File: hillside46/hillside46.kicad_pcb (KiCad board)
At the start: 2 copper layers, 142.5 x 99.9 mm, 92 parts, among them J1 Haptic, J2 TRRS, J3 Bat_Pos, J4 Bat_Neg, J5 Bat_Pos, J6 Bat_Neg, K1 SW_Key, K10 SW_Key, K11 SW_Key, K12 SW_Key, K13 SW_Key, K14 SW_Key, K15 SW_Key, K16 SW_Key, K17 SW_Key, K18 SW_Key, K19 SW_Rotary, K2 SW_Key, K20 SW_Rotary, K21 SW_Key, K22 SW_Key, K23 SW_Key, K3 SW_Key, K4 SW_Key, K5 SW_Key, K6 SW_Key, K7 SW_Key, K8 SW_Key, K9 SW_Key, SW1 SKQGAFE010, SW2 SW_Power, U1 ProMicro_r, U2 SRV05-4

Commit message: my mods
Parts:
- removed D1, D2, D3, D4: SK6812-MINI-E, hillside_basic:SK6812-MINI-E
- removed D19, D20, D21: BAV70, hillside_basic:SOT-23
- removed H1: Mount_Tenting, hillside:Tenting_Puck
- removed H26, H27, H28, H29, H30, H31: Breakoff Hole, hillside_basic:HoleBreakoff_1mm
- removed H3: Logo, hillside:Hillside_Logo
- added D16: 1N4148W, Diode_SMD:D_SOD-123, F.Cu at (89.6, 103.9)
- added D17: 1N4148W, Diode_SMD:D_SOD-123, F.Cu at (107.3, 100.7)
- added D18: 1N4148W, Diode_SMD:D_SOD-123, F.Cu at (124.0, 85.6)
- added D22: 1N4148W, Diode_SMD:D_SOD-123, F.Cu at (142.5, 78.5)
- added D23: 1N4148W, Diode_SMD:D_SOD-123, F.Cu at (160.5, 84.0)
- added D24: 1N4148W, Diode_SMD:D_SOD-123, F.Cu at (178.5, 69.6)
- added D25: 1N4148W, Diode_SMD:D_SOD-123, F.Cu at (178.5, 86.5)
- added D26: 1N4148W, Diode_SMD:D_SOD-123, F.Cu at (170.8, 104.0)
- added D27: 1N4148W, Diode_SMD:D_SOD-123, F.Cu at (190.3, 112.1)
- added D28: 1N4148W, Diode_SMD:D_SOD-123, F.Cu at (207.0, 125.0)
- added D29: 1N4148W, Diode_SMD:D_SOD-123, F.Cu at (198.8, 97.5)
- added D30: 1N4148W, Diode_SMD:D_SOD-123, F.Cu at (150.0, 101.0)
- added D5: 1N4148W, Diode_SMD:D_SOD-123, F.Cu at (83.7, 70.5)
- added D6: 1N4148W, Diode_SMD:D_SOD-123, F.Cu at (86.7, 87.2)
- D10, D11, D12, D13, D14, D15, D7, D8, D9: value BAV70 -> 1N4148W; footprint hillside_basic:SOT-23 -> Diode_SMD:D_SOD-123
- K19, K20: value SW_Rotary -> SW_Key; footprint hillside:pg1350-DR_rotary_hotswap -> hillside:pg1350-R_hotswap
- moved D13 79.2 mm to (160.5, 49.9), turned to 180 degrees
- moved D14 40.9 mm to (160.5, 67.0), turned to 180 degrees
- moved D9 39.5 mm to (121.0, 51.6), turned to -175 degrees
- moved D8 36.4 mm to (104.4, 84.0), turned to -170 degrees
- moved D15 36.3 mm to (178.5, 52.5), turned to 180 degrees
- moved D11 31.2 mm to (142.5, 44.5), turned to 180 degrees
- moved D10 23.8 mm to (122.5, 68.6), turned to -175 degrees
- moved D12 18.8 mm to (142.5, 61.5), turned to 180 degrees
- moved K20 4.51 mm to (150.0, 105.7), turned to 180 degrees
- moved K19 4.50 mm to (196.5, 101.5)
- turned D7 to -170 degrees
- turned K13 to -170 degrees
- turned K14 to -170 degrees
- turned K21 to 165 degrees
- turned K23 to 135 degrees
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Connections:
- D10 pad 1: Net-(D10-Pad1) -> row1
- D10 pad 2: Net-(D10-Pad2) -> Net-(D10-A)
- D11 pad 1: Net-(D11-Pad1) -> row0
- D11 pad 2: Net-(D11-Pad2) -> Net-(D11-A)
- D12 pad 1: Net-(D12-Pad1) -> row1
- D12 pad 2: Net-(D12-Pad2) -> Net-(D12-A)
- D13 pad 1: Net-(D13-Pad1) -> row0
- D13 pad 2: Net-(D13-Pad2) -> Net-(D13-A)
- D14 pad 1: Net-(D14-Pad1) -> row1
- D14 pad 2: Net-(D14-Pad2) -> Net-(D14-A)
- D15 pad 1: Net-(D15-Pad1) -> row0
- D15 pad 2: Net-(D15-Pad2) -> Net-(D15-A)
- D7 pad 1: Net-(D7-Pad1) -> row0
- D8 pad 1: Net-(D8-Pad1) -> row1
- D8 pad 2: Net-(D8-Pad2) -> Net-(D8-A)
- D9 pad 1: Net-(D9-Pad1) -> row0
- D9 pad 2: Net-(D9-Pad2) -> Net-(D9-A)
- JP2 pad 2: Net-(D19-Pad2) -> row3
- K1 pad 2: Net-(D7-Pad1) -> Net-(D5-A)
- K10 pad 2: Net-(D11-Pad2) -> Net-(D12-A)
- K11 pad 2: Net-(D12-Pad1) -> Net-(D14-A)
- K12 pad 2: Net-(D12-Pad2) -> Net-(D24-A)
- K13 pad 2: Net-(D13-Pad1) -> Net-(D16-A)
- K14 pad 2: Net-(D13-Pad2) -> Net-(D17-A)
- K15 pad 2: Net-(D14-Pad1) -> Net-(D18-A)
- K16 pad 2: Net-(D14-Pad2) -> Net-(D22-A)
- K17 pad 2: Net-(D15-Pad1) -> Net-(D23-A)
- K18 pad 2: Net-(D15-Pad2) -> Net-(D25-A)
- K3 pad 2: Net-(D8-Pad1) -> Net-(D9-A)
- K4 pad 2: Net-(D8-Pad2) -> Net-(D11-A)
- K5 pad 2: Net-(D9-Pad1) -> Net-(D13-A)
- K6 pad 2: Net-(D9-Pad2) -> Net-(D15-A)
- K7 pad 2: Net-(D10-Pad1) -> Net-(D6-A)
- K8 pad 2: Net-(D10-Pad2) -> Net-(D8-A)
- K9 pad 2: Net-(D11-Pad1) -> Net-(D10-A)
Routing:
- net enc_a: track 141.4 -> 0.00 mm, vias 4 -> 0
- net enc_b: track 138.5 -> 0.00 mm, vias 4 -> 0
- net VCC_ACC: track 127.0 -> 42.8 mm, vias 5 -> 1
- net LED: track 62.2 -> 0.00 mm, vias 3 -> 0
- net row3: track 121.8 -> 179.0 mm, vias 3 -> 7
- net (no net): track 0.00 -> 40.1 mm, vias 0 -> 2
- net row0: track 129.7 -> 165.0 mm, vias 3 -> 8
- net Net-(D21-Pad1): track 29.1 -> 0.00 mm, vias 1 -> 0
- net Net-(D1-Pad2): track 27.8 -> 0.00 mm, vias 6 -> 0
- net Net-(D19-Pad2): track 26.8 -> 0.00 mm
- net row2: track 119.7 -> 146.0 mm, vias 3 -> 9
- net GND: track 74.5 -> 49.1 mm, vias 6 -> 2
- net Net-(D7-Pad1): track 23.0 -> 0.00 mm, vias 1 -> 0
- net row1: track 116.4 -> 138.6 mm, vias 2 -> 9
- net Net-(D3-Pad2): track 21.4 -> 0.00 mm, vias 3 -> 0
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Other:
- outline, holes or cut-outs redrawn
- board text removed: "0.1.0"
- board text removed: "Hillside 46"
- board text removed: "PCB by MM"

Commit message: trrs changes
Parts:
- removed H25: ToolingHole, hillside_basic:ToolingHole_1.152mm
- D10, D11, D12, D13, D14, D15, D16, D17, D18, D22, D23, D24, D25, D26, D27, D28, D29, D30, D5, D6, D7, D8, D9: footprint Diode_SMD:D_SOD-123 -> hillside:D_SOD-123_Hillside_reversable
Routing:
- net row3: track 179.0 -> 156.4 mm, vias 7 -> 3
- net Net-(D14-A): track 0.00 -> 9.71 mm
- net Net-(D23-A): track 0.00 -> 9.42 mm
- net Net-(D22-A): track 0.00 -> 9.39 mm
- net Net-(D26-A): track 19.6 -> 10.4 mm
- net row1: track 138.6 -> 146.1 mm, vias 9 -> 3
- net col2: track 164.5 -> 168.5 mm
- net Net-(D12-A): track 13.3 -> 9.54 mm
- net row2: track 146.0 -> 148.7 mm, vias 9 -> 4
- net VCC: track 91.9 -> 93.7 mm
- net data: track 95.5 -> 97.1 mm
- net Net-(D10-A): track 8.12 -> 9.72 mm
- net col3: track 154.3 -> 155.6 mm
- net row0: track 165.0 -> 164.4 mm, vias 8 -> 5

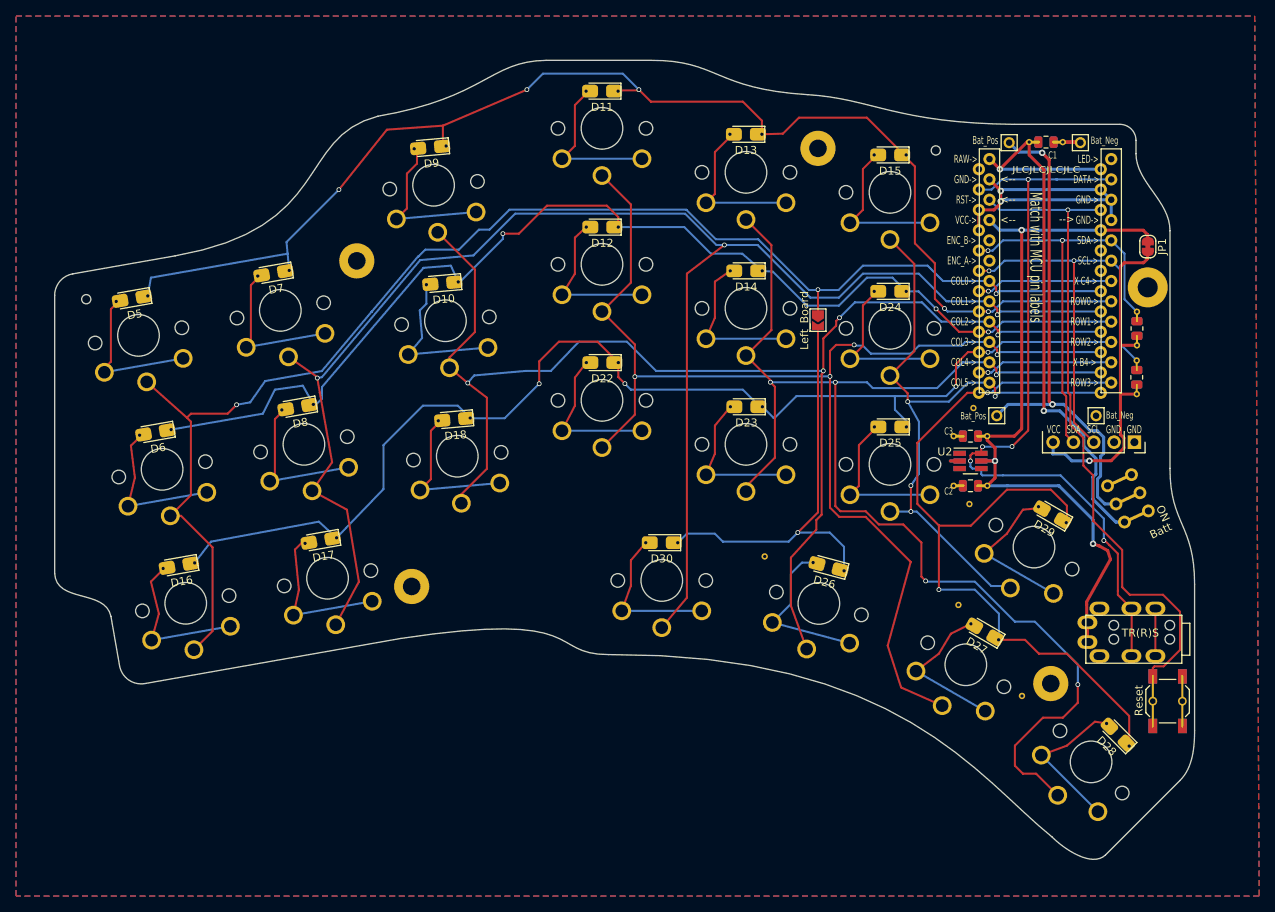
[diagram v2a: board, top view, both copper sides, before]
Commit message: usb-c switch changes
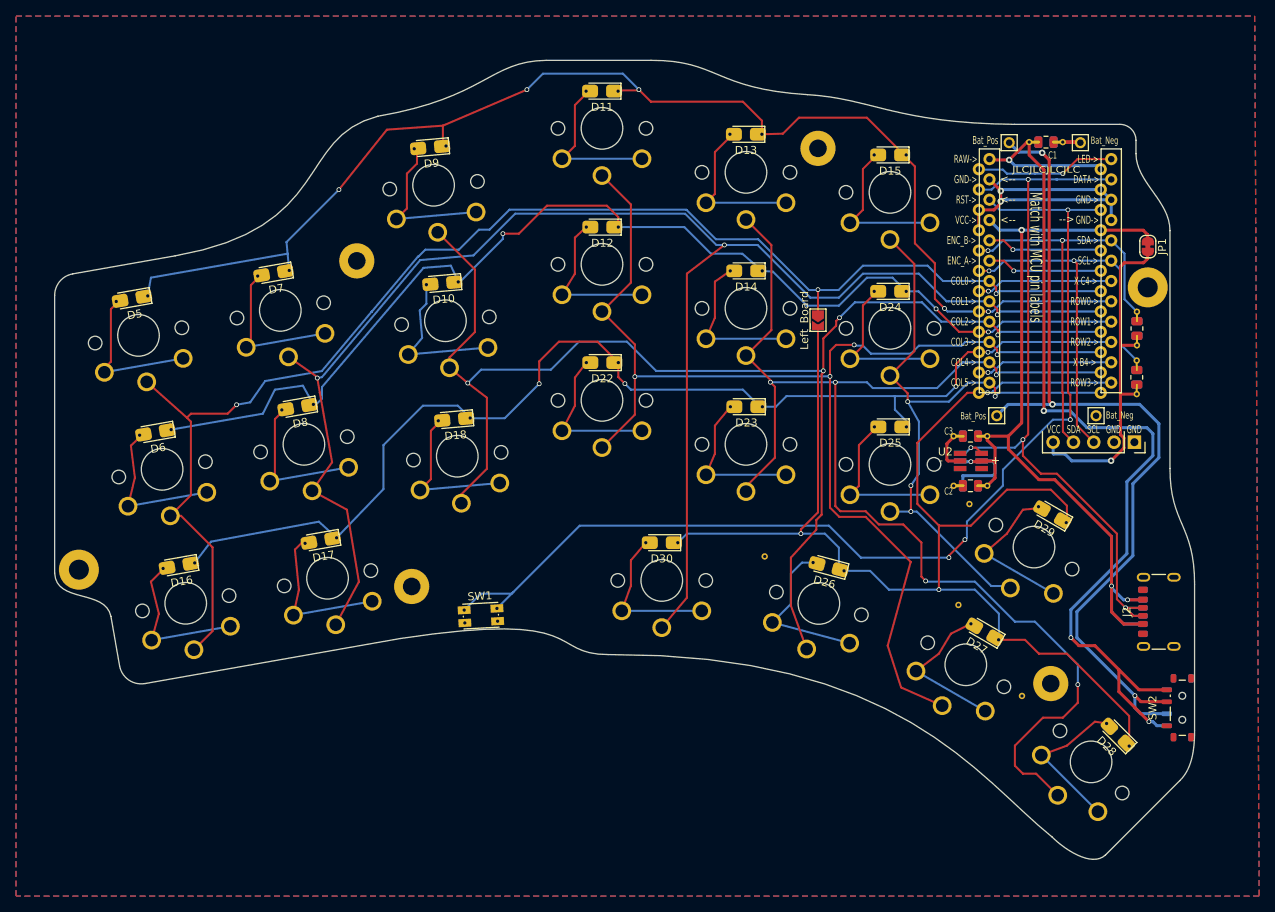
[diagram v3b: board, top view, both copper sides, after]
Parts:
- removed H10, H11, H12, H13, H14, H15, H16, H17, H18, H19, H2, H20, H21, H22, H9: Bumpon, hillside:Bumpon
- removed H23, H24: ToolingHole, hillside_basic:ToolingHole_1.152mm
- removed V2: Via, hillside_basic:VIA-0.8mm
- added ?: , , F.Cu at (77.1, 104.4)
- J2: value TRRS -> USB_C_Receptacle_PowerOnly_6P; footprint hillside:MJ-4PP-9 -> hillside:USB_C_Receptacle_GCT_USB4125-xx-x-0190_6P_TopMnt_Horizontal
- SW1: footprint hillside_basic:SW_SPST_SKQG_WithStem -> hillside:SW_Push_1P1T_NO_CK_KMR2
- SW2: footprint hillside_basic:SW_SPDT_JS202011AQN -> hillside:SW_SPDT_Shouhan_MSK12C02
- moved SW1 86.5 mm to (127.4, 110.1), turned to 3 degrees
- moved SW2 27.0 mm to (215.0, 121.6), turned to 90 degrees
- moved J2 10.8 mm to (213.2, 109.6)
- moved U2 0.06 mm to (188.6, 90.8)
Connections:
- net LED renamed led
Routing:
- net reset: track 83.1 -> 135.1 mm, vias 1 -> 4
- net raw: track 74.1 -> 122.4 mm, vias 2 -> 4
- net bat+: track 62.7 -> 109.8 mm, vias 2 -> 3
- net led: track 0.00 -> 17.5 mm, vias 0 -> 1
- net VCC: track 93.7 -> 109.3 mm, vias 3 -> 4
- net enc_a: track 0.00 -> 14.5 mm, vias 0 -> 1
- net enc_b: track 0.00 -> 14.4 mm, vias 0 -> 1
- net row3: track 156.4 -> 167.9 mm
- net GND: track 49.1 -> 60.1 mm
- net (no net): track 40.1 -> 34.2 mm
- net row2: track 148.7 -> 147.6 mm
- net data: track 97.1 -> 97.2 mm, vias 5 -> 4

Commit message: usb-c switch changes
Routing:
- net VCC: track 109.3 -> 107.9 mm
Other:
- board text removed: "-2-"
- board text removed: "-br-"
- board text removed: "-cut 1-"
- board text removed: "-cut 2-"
- board text removed: "-cut 3-"
- board text removed: "-cut Z-"
- board text removed: "CUT"
- board text removed: "CUT OUT"
- board text removed: "cut Y-"
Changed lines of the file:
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@@
 		(grid_origin 148.604829 78.853153)
 		(pcbplotparams
-			(layerselection 0x00000000_00000000_5555555f_f7d5f5ff)
+			(layerselection 0x00000000_00000000_55555555_575555ff)
 			(plot_on_all_layers_selection 0x00000000_00000000_00000000_00000000)
 			(disableapertmacros no)
-			(usegerberextensions no)
+			(usegerberextensions yes)
 			(usegerberattributes yes)
 			(usegerberadvancedattributes yes)
@@
 			(drillshape 0)
 			(scaleselection 1)
-			(outputdirectory "./gerber_hillside46")
+			(outputdirectory "gerbers/")
 		)
 	)
@@
 		)
 	)
-	(gr_text "CUT OUT"
-		(at 83.696901 83.270599 0)
-		(layer "F.Fab")
-		(effects
-			(font
-				(size 1 1)
-				(thickness 0.2)
-			)
-		)
-	)
-	(gr_text "CUT OUT"
-		(at 84.554829 95.403153 0)
-		(layer "F.Fab")
-		(effects
-			(font
-				(size 1 1)
-				(thickness 0.2)
-			)
-		)
-	)
-	(gr_text "CUT OUT"
-		(at 91.854829 111.403153 10)
-		(layer "F.Fab")
-		(effects
-			(font
-				(size 1 1)
-				(thickness 0.2)
-			)
-		)
-	)
-	(gr_text "CUT OUT"
-		(at 92.454829 77.103153 90)
-		(layer "F.Fab")
-		(effects
-			(font
-				(size 1 1)
-				(thickness 0.2)
-			)
-		)
-	)
-	(gr_text "CUT OUT"
-		(at 92.500867 99.311877 90)
-		(layer "F.Fab")
-		(effects
-			(font
-				(size 1 1)
-				(thickness 0.2)
-			)
-		)
-	)
-	(gr_text "CUT OUT"
-		(at 96.300866 89.411877 100)
-		(layer "F.Fab")
-		(effects
-			(font
-				(size 1 1)
-				(thickness 0.2)
-			)
-		)
-	)
-	(gr_text "CUT"
-		(at 99.154829 105.653153 100)
-		(layer "F.Fab")
-		(effects
-			(font
-				(size 1 1)
-				(thickness 0.2)
-			)
-		)
-	)
-	(gr_text "-cut Z-"
-		(at 94.854829 85.303153 -20)
-		(layer "User.3")
-		(effects
-			(font
-				(size 1 1)
-				(thickness 0.15)
-			)
-		)
-	)
-	(gr_text "-cut A-"
-		(at 76.704829 83.103153 0)
-		(layer "User.3")
-		(effects
-			(font
-				(size 1 1)
-				(thickness 0.15)
-			)
-		)
-	)
-	(gr_text "-cut 2-"
-		(at 76.954829 95.403153 0)
-		(layer "User.3")
-		(effects
-			(font
-				(size 1 1)
-				(thickness 0.15)
-			)
-		)
-	)
-	(gr_text "-br-"
-		(at 90.004829 95.453153 0)
-		(layer "User.3")
-		(effects
-			(font
-				(size 1 1)
-				(thickness 0.15)
-			)
-		)
-	)
-	(gr_text "-br-"
-		(at 90.473885 83.241236 0)
-		(layer "User.3")
-		(effects
-			(font
-				(size 1 1)
-				(thickness 0.15)
-			)
-		)
-	)
-	(gr_text "-cut 1-"
-		(at 84.454829 112.653153 10)
-		(layer "User.3")
-		(effects
-			(font
-				(size 1 1)
-				(thickness 0.15)
-			)
-		)
-	)
-	(gr_text "-br-"
-		(at 97.304829 109.853153 10)
-		(layer "User.3")
-		(effects
-			(font
-				(size 1 1)
-				(thickness 0.15)
-			)
-		)
-	)
-	(gr_text "cut Y-"
-		(at 94.354829 94.203153 25)
-		(layer "User.3")
-		(effects
-			(font
-				(size 1 1)
-				(thickness 0.15)
-			)
-		)
-	)
-	(gr_text "-2-"
-		(at 92.204829 103.853153 90)
-		(layer "User.3")
-		(effects
-			(font
-				(size 1 1)
-				(thickness 0.15)
-			)
-		)
-	)
 	(gr_text "-cut A-"
 		(at 92.354829 66.591236 90)
@@
 		)
 	)
-	(gr_text "-cut 2-"
-		(at 92.854829 109.203153 100)
-		(layer "User.3")
-		(effects
-			(font
-				(size 1 1)
-				(thickness 0.15)
-			)
-		)
-	)
-	(gr_text "-cut 1-"
-		(at 100.354829 112.853153 100)
-		(layer "User.3")
-		(effects
-			(font
-				(size 1 1)
-				(thickness 0.15)
-			)
-		)
-	)
-	(gr_text "-cut 3-"
-		(at 95.654829 102.203153 350)
-		(layer "User.3")
-		(effects
-			(font
-				(size 1 1)
-				(thickness 0.15)
-			)
-		)
-	)
 	(segment
 		(start 190.731813 79.701068)
@@
 	)
 	(segment
-		(start 193.294059 87.663923)
-		(end 193.294059 89.292383)
-		(width 0.381)
-		(layer "F.Cu")
-		(net "VCC")
-	)
-	(segment
-		(start 199.087329 93.103153)
-		(end 206.184829 100.200653)
-		(width 0.381)
-		(layer "F.Cu")
-		(net "VCC")
-	)
-	(segment
 		(start 194.950866 61.909063)
 		(end 194.950866 86.007116)
@@
 	)
 	(segment
-		(start 197.104829 93.103153)
-		(end 199.087329 93.103153)
-		(width 0.381)
-		(layer "F.Cu")
-		(net "VCC")
-	)
-	(segment
 		(start 193.294059 87.663923)
 		(end 190.6482 87.663923)
@@
 	)
 	(segment
+		(start 199.087329 93.103153)
+		(end 206.184829 100.200653)
+		(width 0.381)
+		(layer "F.Cu")
+		(net "VCC")
+	)
+	(segment
 		(start 191.619922 92.8922)
 		(end 190.648201 93.863921)
@@
 	)
 	(segment
-		(start 193.294059 89.292383)
-		(end 197.104829 93.103153)
+		(start 206.184829 100.200653)
+		(end 206.184829 106.390653)
 		(width 0.381)
 		(layer "F.Cu")
@@
 	)
 	(segment
+		(start 191.619922 92.8922)
+		(end 191.830875 93.103153)
+		(width 0.381)
+		(layer "F.Cu")
+		(net "VCC")
+	)
+	(segment
 		(start 189.8656 90.853153)
 		(end 189.954829 90.763924)
@@
 	)
 	(segment
+		(start 191.830875 93.103153)
+		(end 199.087329 93.103153)
+		(width 0.381)
+		(layer "F.Cu")
+		(net "VCC")
+	)
+	(segment
 		(start 206.184829 109.623153)
 		(end 206.184829 106.390653)
@@
 	)
 	(segment
-		(start 206.184829 100.200653)
-		(end 206.184829 106.390653)
-		(width 0.381)
-		(layer "F.Cu")
-		(net "VCC")
-	)
-	(segment
 		(start 207.704829 111.143153)
 		(end 206.184829 109.623153)
@@
 		(net "data")
 	)
-	(segment
-		(start 187.294058 89.853153)
-		(end 187.254829 89.813924)
-		(width 0.254)
-		(layer "F.Cu")
-		(net "unconnected-(U2-IO4-Pad1)_1")
-	)
 	(zone
